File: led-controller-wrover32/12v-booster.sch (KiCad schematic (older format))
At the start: 16 parts, among them J101 Conn_01x02 DNS, U101 TPS55340-Q1

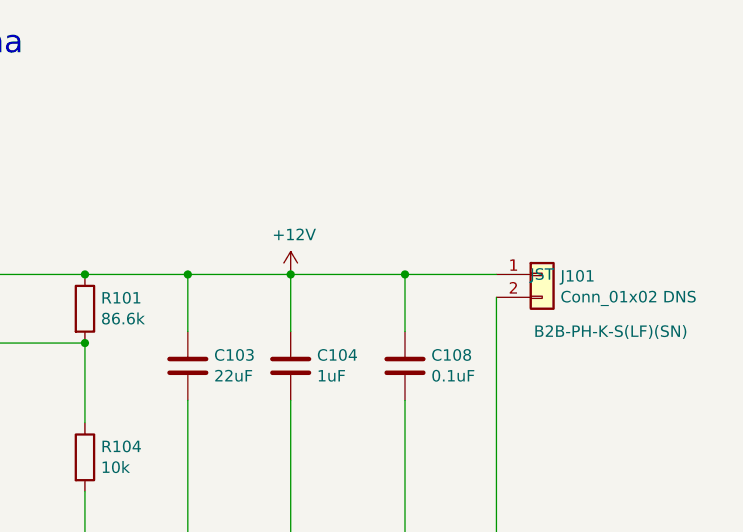
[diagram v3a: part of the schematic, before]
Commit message: Version 3.0.0
- Added speaker output support
- Added 22 ohm resistors on 5V I/O
- Changed from 2 to 4 layers
- Added boot button
- Added 12V to PWM output
- Added 5V protection diode

Signed-off-by: aaronw <aaron.w2@gmail.com>
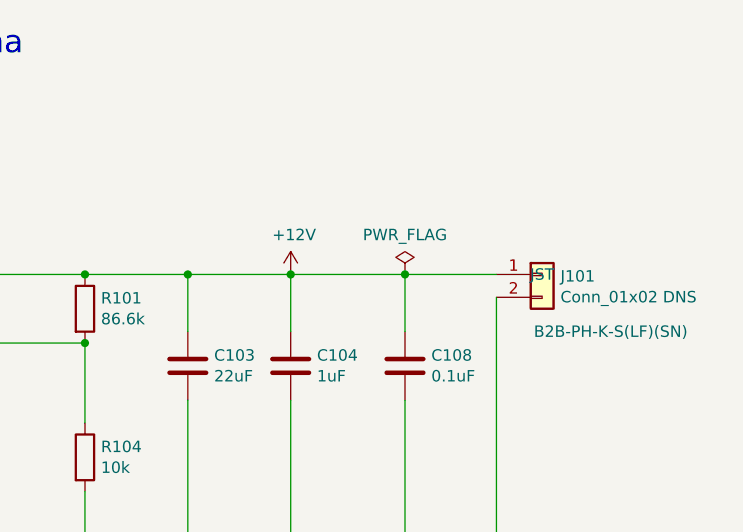
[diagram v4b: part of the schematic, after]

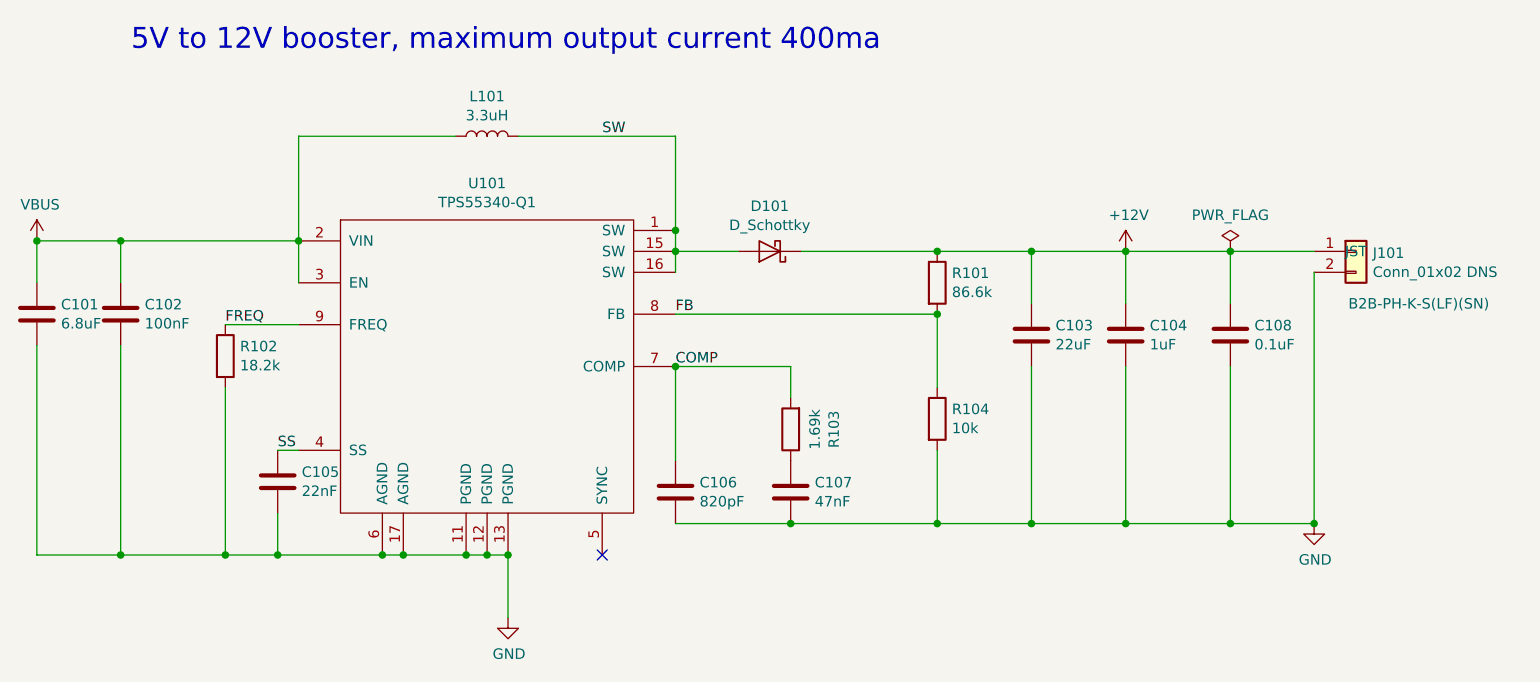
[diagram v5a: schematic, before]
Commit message: Fix reset circuit and other stuff
This fixes the reset circuit and moves a few components.  It also
cleans up the BOM a bit.

Also bumped to version 3.5.0

Signed-off-by: Aaron Williams <aaron.w2@gmail.com>
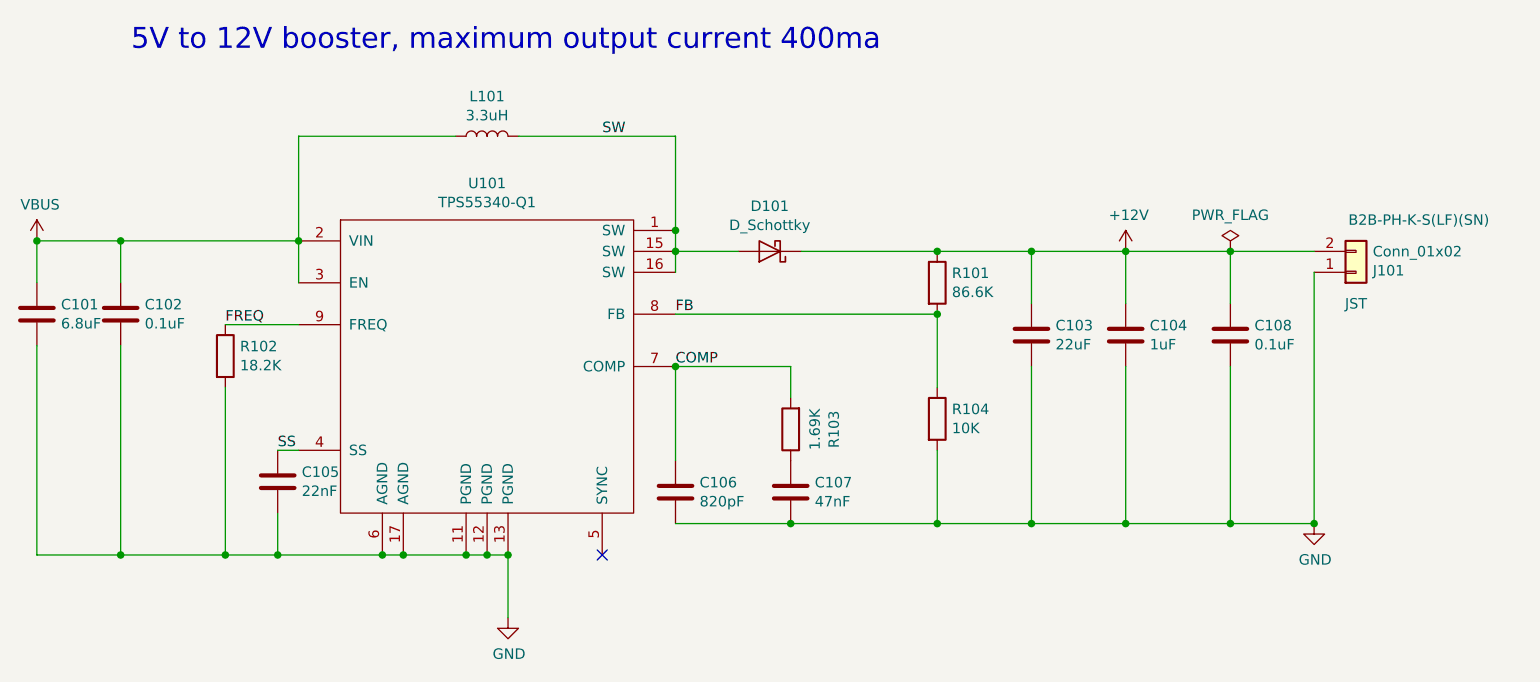
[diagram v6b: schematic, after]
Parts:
- C102: value 100nF -> 0.1uF
- J101: value Conn_01x02 DNS -> Conn_01x02
- R101: value 86.6k -> 86.6K
- R102: value 18.2k -> 18.2K
- R103: value 1.69k -> 1.69K
- R104: value 10k -> 10K
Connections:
- net +12V: now also J101.2 (Pin_2); no longer J101.1 (Pin_1)
- net GND: now also J101.1 (Pin_1); no longer J101.2 (Pin_2)

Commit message: Moved WS2813B after fixing footprint  v3.6
Signed-off-by: Aaron Williams <aaron.w2@gmail.com>
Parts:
- C102: MFR Samsung -> Murata Electronics; MPN CL10B104KO8WPNC -> GCM188R71H104KA57D; SPN 1276-6582-1-ND -> 490-4779-1-ND
- C105: MFR Samsung -> Yageo; MPN CL10B223KB8WPNC -> CC0603JRX7R9BB223; SPN 1276-6534-1-ND -> 311-4010-1-ND; SPURL - -> https://www.digikey.com/product-detail/en/yageo/CC0603JRX7R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
- C106: MFR Kemet -> Yageo; MPN C0603C821J5RACTU -> CC0603JRNPO9BN821; SPN 399-9127-1-ND -> 311-1775-1-ND; SPURL - -> https://www.digikey.com/products/en?keywords=311-1775-1-ND
- C108: MFR AVX -> Murata Electronics; MPN 06035C104K4Z4A -> GCM188R71H104KA57D; SPN 478-10679-1-ND -> 490-4779-1-ND; SPURL https://www.digikey.com/product-detail/en/avx-corporation/0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 -> https://www.digikey.com/product-detail/en/murata-electronic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
